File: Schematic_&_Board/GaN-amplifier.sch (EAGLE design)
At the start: 52 parts, among them IC1 LT3080, Q1 MMBT3906LT1SMD, T1 IRL3714S, T2 IRL3714S, T3 IRL3714S, U1 TPS7A30XX, U2 HMC1099, U3 LT1783, U4 CPC1117NTR, U5 LT1783, U6 LTC2924, U7 LCA701S, X1 SMA-142-0701-801/806, X2 SMA-142-0701-801/806

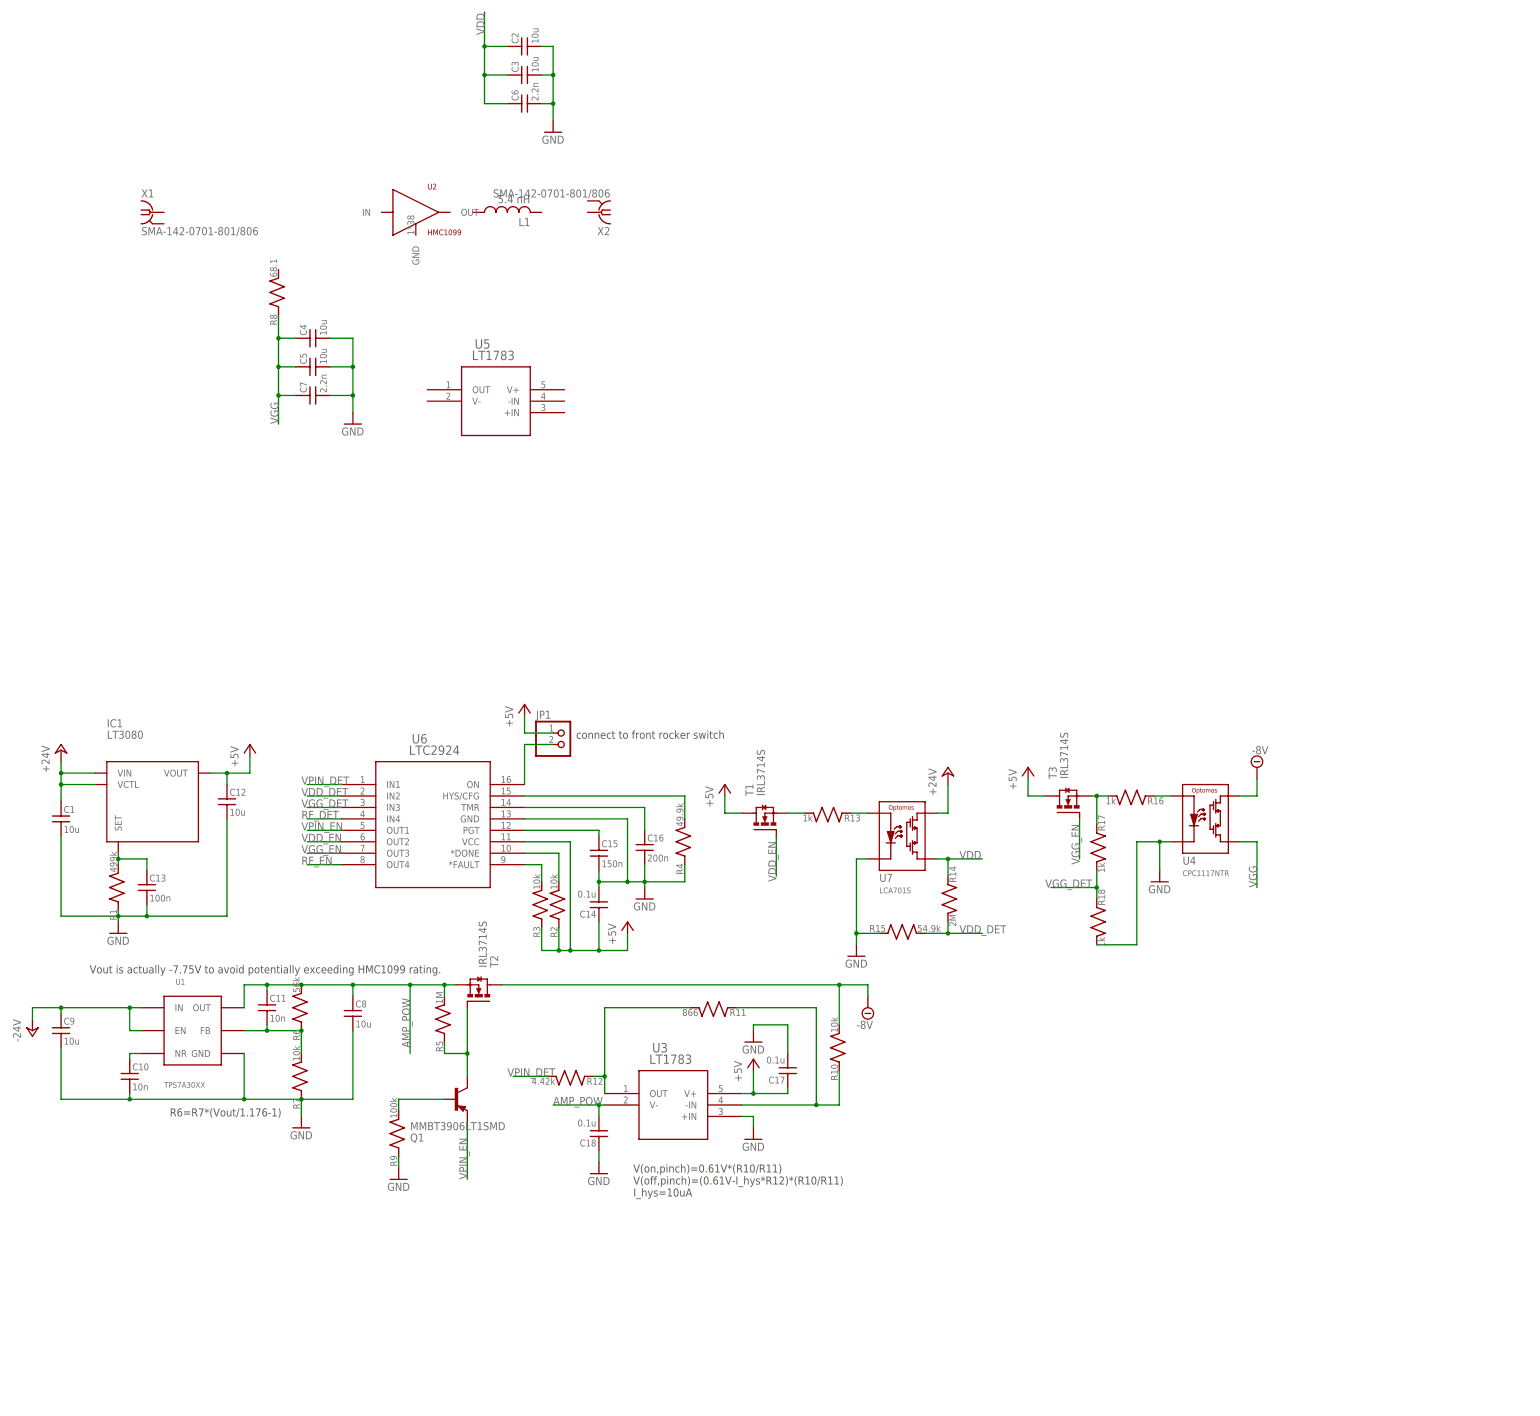
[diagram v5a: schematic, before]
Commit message: Finished Power Sequencing
Completed the power sequencing section. Starting on the RF amp section.
Need to track down the correct inductors.

DSB
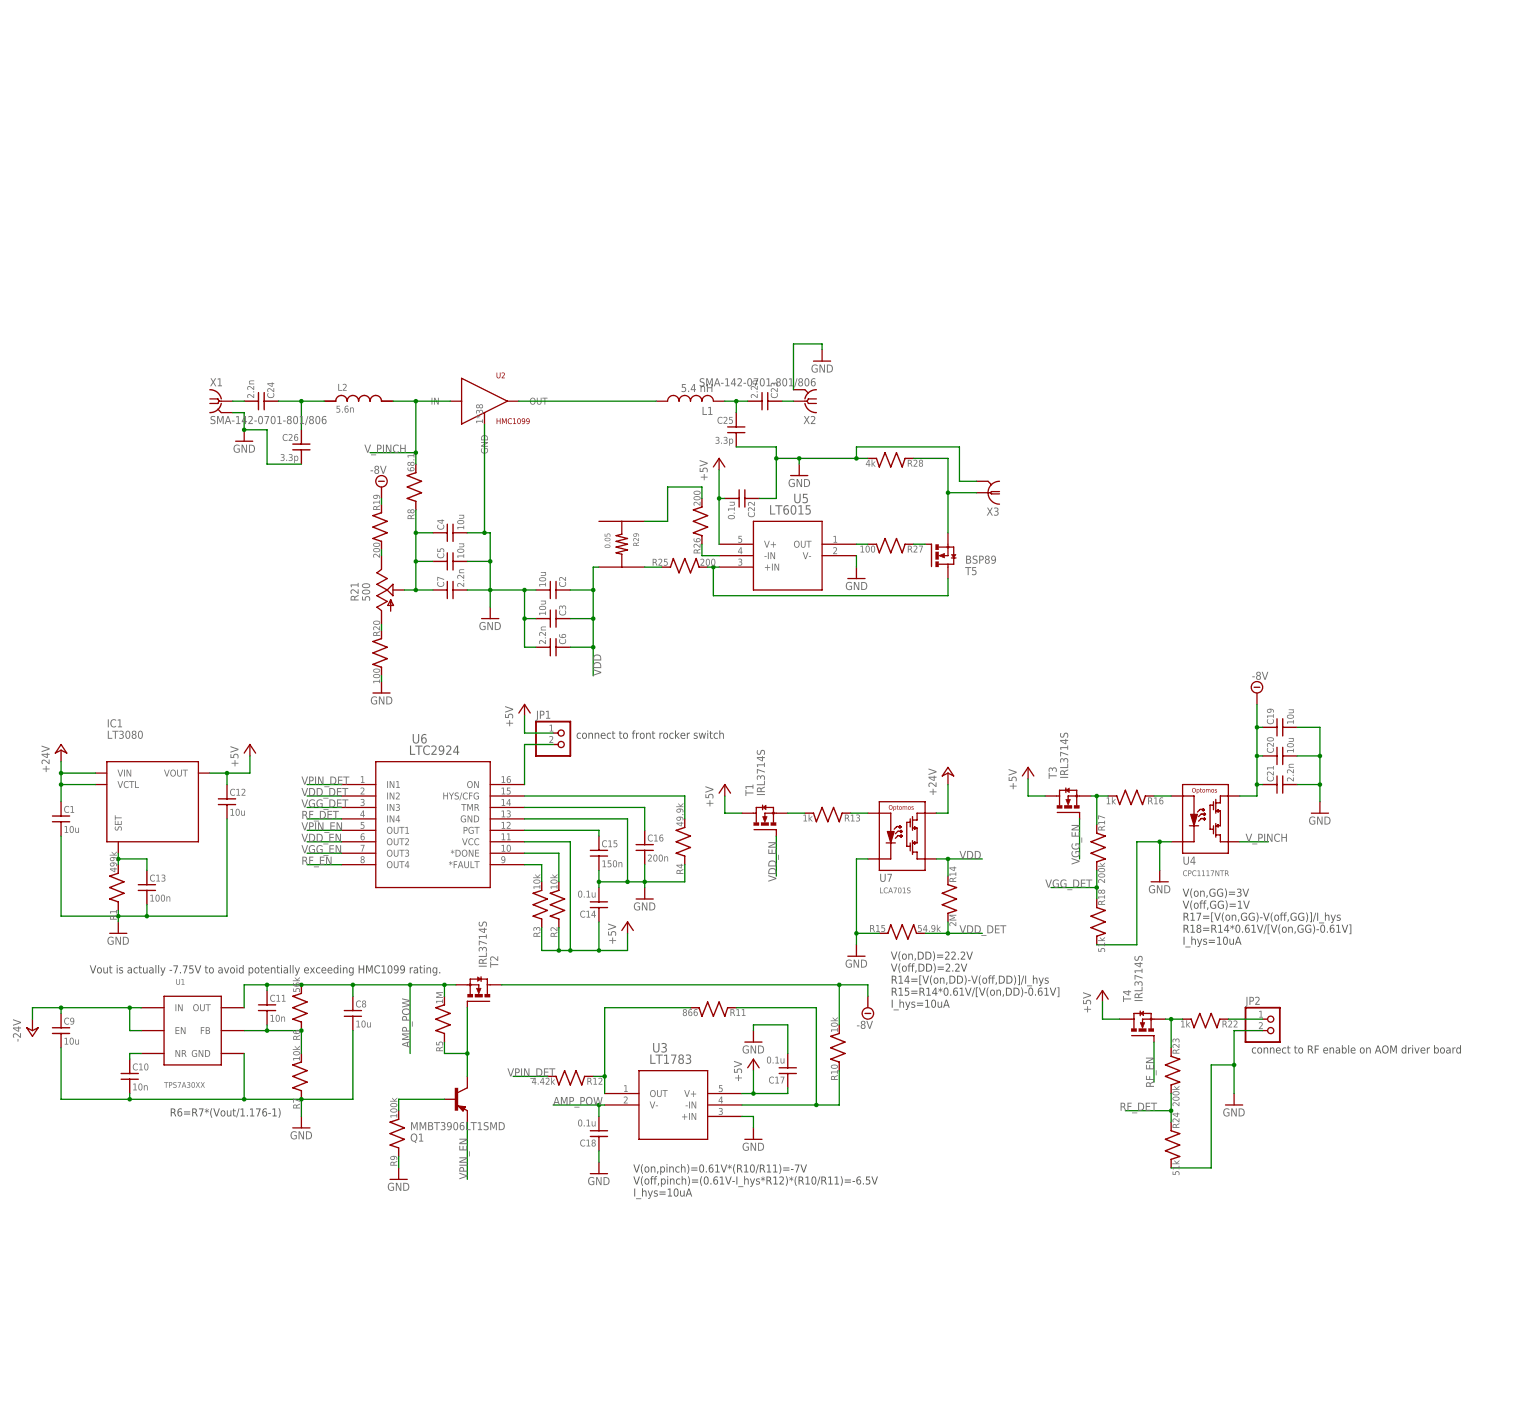
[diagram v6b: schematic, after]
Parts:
- added C19, C20: 10u, jqi_passives:C_MLCC_SMDCMLCC_1210
- added C21, C23, C24: 2.2n, jqi_passives:C_MLCC_SMDCMLCC_0603
- added C22: 0.1u, jqi_passives:C_MLCC_SMDCMLCC_0603
- added C25, C26: 3.3p, jqi_passives:C_MLCC_SMDCMLCC_0603
- added JP2: (no value), pinhead:PINHD-1X2
- added L2: 5.6n, jqi_passives:L_FERRITE_SMDLFERRITE_0402
- added R19, R25, R26: 200, jqi_passives:R_SMDR0603
- added R20, R27: 100, jqi_passives:R_SMDR0603
- added R21: 500, rlc-jqi:BOURNS-3269P
- added R22: 1k, jqi_passives:R_SMDR0603
- added R23: 200k, jqi_passives:R_SMDR0603
- added R24: 51k, jqi_passives:R_SMDR0603
- added R28: 4k, jqi_passives:R_SMDR0603
- added R29: 0.05, rlc-jqi:RES_KELVIN
- added T4: IRL3714S, transistor-jqi:IRL3714
- added T5: BSP89, transistor-jqi:BSP89
- added X3: BNC-V, connector-jqi:BNC-V
- R17: value 1k -> 200k
- R18: value 1k -> 51k
- U5: value LT1783 -> LT6015; device linear-technology-jqi:LT1783HS5 -> linear-technology-jqi:LT6015HS5
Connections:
- removed net VGG: C4.1, C5.1, C7.1, R8.1, U4.P$3
- new net N$18: C4.1, C5.1, C7.1, R21.2, R8.1
- new net N$19: R19.2, R21.3
- new net N$20: R20.1, R21.1
- new net N$21: R22.2, R23.1, T4.S
- new net N$22: JP2.1, R22.1
- new net N$23: R26.1, U5.-IN
- new net N$24: R25.2, T5.D, U5.+IN
- new net N$25: R27.2, U5.OUT
- new net N$26: R27.1, T5.G
- new net N$27: R25.1, R29.V$2
- new net N$28: R28.1, T5.S, X3.1
- new net N$29: R26.2, R29.V$1
- new net N$30: C23.1, X2.1
- new net N$31: C24.2, X1.1
- new net N$33: C23.2, C25.1, L1.2
- new net N$34: L1.1, U2.OUT
- new net N$35: C24.1, C26.1, L2.1
- new net V_PINCH: L2.2, R8.2, U2.IN, U4.P$3
- net +5V: now also C22.2, T4.D, U5.V+
- net -8V: now also C19.1, C20.1, C21.1, R19.1
- net GND: now also C19.2, C20.2, C21.2, C22.1, C25.2, C26.2, JP2.2, R20.2, R24.2, R28.2, U2.GND, U5.V-, X1.2, X2.2, X3.2
- net RF_DET: now also R23.2, R24.1
- net RF_EN: now also T4.G
- net VDD: now also R29.I$2
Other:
- note added: "V(on,DD)=22.2V V(off,DD)=2.2V R14=[V(on,DD)-V(off,DD)]/I_hys R15=R14*0.61V/[V(on,DD)-0.61V] I_hys=10uA"
- note added: "V(on,GG)=3V V(off,GG)=1V R17=[V(on,GG)-V(off,GG)]/I_hys R18=R14*0.61V/[V(on,GG)-0.61V] I_hys=10uA"
- note added: "V(on,pinch)=0.61V*(R10/R11)=-7V V(off,pinch)=(0.61V-I_hys*R12)*(R10/R11)=-6.5V I_hys=10uA"
- note added: "connect to RF enable on AOM driver board"
- note removed: "V(on,pinch)=0.61V*(R10/R11) V(off,pinch)=(0.61V-I_hys*R12)*(R10/R11) I_hys=10uA"
- moved on the sheet: C2, C3, C4, C5, C6, C7, L1, R8, U2, X1, X2

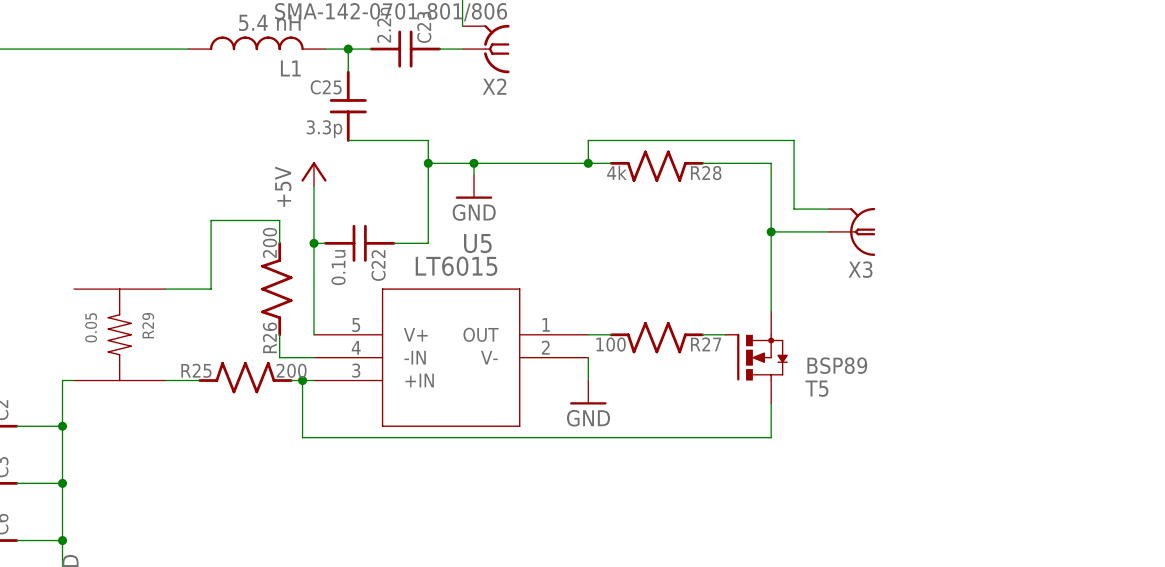
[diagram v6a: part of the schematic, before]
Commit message: Mostly done with schematic
Just need to find that damn bias-t inductor.

DSB
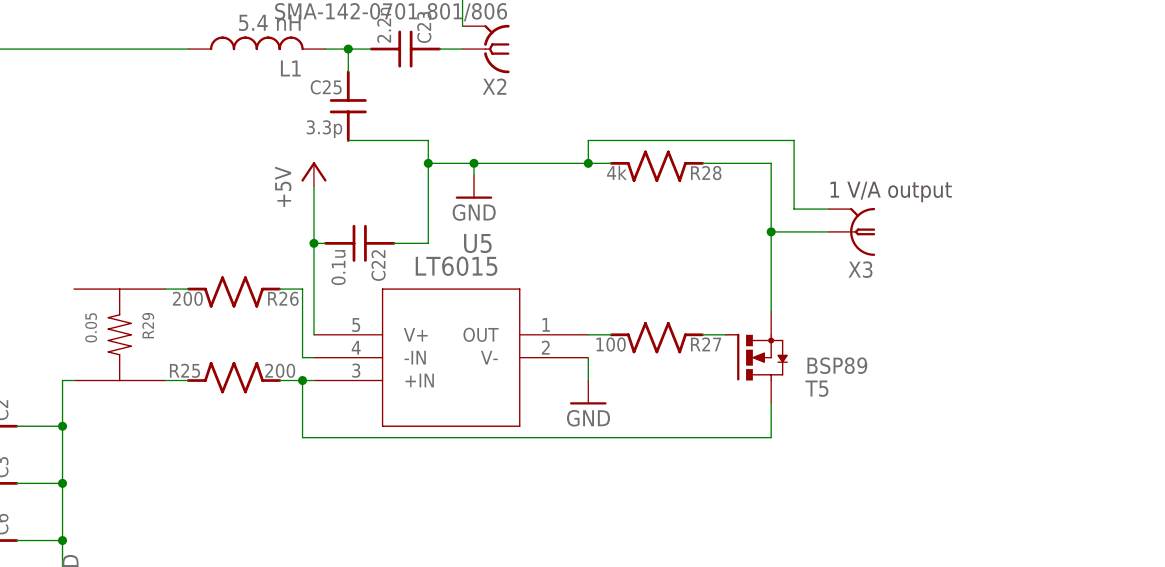
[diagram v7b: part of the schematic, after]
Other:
- note added: "1 V/A output"
- moved on the sheet: R25, R26
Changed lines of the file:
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@@
 I_hys=10uA</text>
 <text x="210.82" y="76.2" size="1.778" layer="97">connect to RF enable on AOM driver board</text>
+<text x="149.86" y="204.47" size="1.778" layer="97">1 V/A output</text>
 </plain>
 <instances>
@@
 <instance part="GND15" gate="1" x="110.49" y="204.47" rot="MR0"/>
 <instance part="GND16" gate="1" x="123.19" y="181.61" rot="MR0"/>
-<instance part="R25" gate="G$1" x="85.09" y="184.15"/>
-<instance part="R26" gate="G$1" x="88.9" y="194.31" rot="R90"/>
+<instance part="R25" gate="G$1" x="83.82" y="184.15"/>
+<instance part="R26" gate="G$1" x="83.82" y="194.31" rot="R180"/>
 <instance part="R27" gate="G$1" x="130.81" y="189.23" rot="R180"/>
 <instance part="R28" gate="G$1" x="130.81" y="208.28" rot="R180"/>
@@
 </segment>
 </net>
-<net name="N$23" class="0">
-<segment>
-<pinref part="R26" gate="G$1" pin="1"/>
-<pinref part="U5" gate="G$1" pin="-IN"/>
-<wire x1="88.9" y1="189.23" x2="88.9" y2="186.69" width="0.1524" layer="91"/>
-<wire x1="88.9" y1="186.69" x2="92.71" y2="186.69" width="0.1524" layer="91"/>
-</segment>
-</net>
 <net name="N$24" class="0">
 <segment>
@@
 <wire x1="92.71" y1="184.15" x2="91.44" y2="184.15" width="0.1524" layer="91"/>
 <pinref part="T5" gate="G$1" pin="D"/>
-<wire x1="91.44" y1="184.15" x2="90.17" y2="184.15" width="0.1524" layer="91"/>
+<wire x1="91.44" y1="184.15" x2="88.9" y2="184.15" width="0.1524" layer="91"/>
 <wire x1="143.51" y1="181.61" x2="143.51" y2="177.8" width="0.1524" layer="91"/>
 <wire x1="143.51" y1="177.8" x2="91.44" y2="177.8" width="0.1524" layer="91"/>
@@
 <pinref part="R29" gate="G$1" pin="V$2"/>
 <pinref part="R25" gate="G$1" pin="1"/>
-<wire x1="76.2" y1="184.15" x2="80.01" y2="184.15" width="0.1524" layer="91"/>
-</segment>
-</net>
-<net name="N$29" class="0">
-<segment>
-<pinref part="R26" gate="G$1" pin="2"/>
-<wire x1="88.9" y1="199.39" x2="88.9" y2="201.93" width="0.1524" layer="91"/>
-<wire x1="88.9" y1="201.93" x2="81.28" y2="201.93" width="0.1524" layer="91"/>
-<pinref part="R29" gate="G$1" pin="V$1"/>
-<wire x1="81.28" y1="201.93" x2="81.28" y2="194.31" width="0.1524" layer="91"/>
-<wire x1="81.28" y1="194.31" x2="76.2" y2="194.31" width="0.1524" layer="91"/>
+<wire x1="76.2" y1="184.15" x2="78.74" y2="184.15" width="0.1524" layer="91"/>
 </segment>
 </net>
@@
 </segment>
 </net>
+<net name="N$23" class="0">
+<segment>
+<pinref part="R29" gate="G$1" pin="V$1"/>
+<pinref part="R26" gate="G$1" pin="2"/>
+<wire x1="76.2" y1="194.31" x2="78.74" y2="194.31" width="0.1524" layer="91"/>
+</segment>
+</net>
+<net name="N$29" class="0">
+<segment>
+<pinref part="R26" gate="G$1" pin="1"/>
+<wire x1="88.9" y1="194.31" x2="91.44" y2="194.31" width="0.1524" layer="91"/>
+<wire x1="91.44" y1="194.31" x2="91.44" y2="186.69" width="0.1524" layer="91"/>
+<pinref part="U5" gate="G$1" pin="-IN"/>
+<wire x1="91.44" y1="186.69" x2="92.71" y2="186.69" width="0.1524" layer="91"/>
+</segment>
+</net>

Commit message: Finished Schematic
Found a bias inductor, so the schematic is finished. I'll want to get
the board layed out this week so that a test piece can be ordered before
Xmas.

DSB
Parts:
- added L3: 0.9u, coilcraft-jqi:1008AF-XX
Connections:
- new net N$32: L3.2, R29.I$1
- net N$34: now also L3.1
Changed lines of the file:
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@@
 <part name="C26" library="jqi_passives" deviceset="C_MLCC_SMD" device="CMLCC_0603" value="3.3p"/>
 <part name="L2" library="jqi_passives" deviceset="L_FERRITE_SMD" device="LFERRITE_0402" value="5.6n"/>
+<part name="L3" library="coilcraft-jqi" deviceset="1008AF-XX" device="" value="0.9u"/>
 </parts>
 <sheets>
@@
 <instance part="C26" gate="G$1" x="0" y="212.09" rot="MR0"/>
 <instance part="L2" gate="G$1" x="12.7" y="220.98"/>
+<instance part="L3" gate="G$1" x="66.04" y="208.28"/>
 </instances>
 <busses>
@@
 <pinref part="U2" gate="G$1" pin="OUT"/>
 <pinref part="L1" gate="G$1" pin="1"/>
-<wire x1="48.26" y1="220.98" x2="78.74" y2="220.98" width="0.1524" layer="91"/>
+<wire x1="48.26" y1="220.98" x2="66.04" y2="220.98" width="0.1524" layer="91"/>
+<pinref part="L3" gate="G$1" pin="1"/>
+<wire x1="66.04" y1="220.98" x2="78.74" y2="220.98" width="0.1524" layer="91"/>
+<wire x1="66.04" y1="215.9" x2="66.04" y2="220.98" width="0.1524" layer="91"/>
+<junction x="66.04" y="220.98"/>
 </segment>
 </net>
@@
 </segment>
 </net>
+<net name="N$32" class="0">
+<segment>
+<pinref part="R29" gate="G$1" pin="I$1"/>
+<pinref part="L3" gate="G$1" pin="2"/>
+<wire x1="66.04" y1="194.31" x2="66.04" y2="200.66" width="0.1524" layer="91"/>
+</segment>
+</net>
